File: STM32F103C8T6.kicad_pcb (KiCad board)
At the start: 2 copper layers, 25.4 x 50.8 mm, 29 parts, among them SW1 SW_Push, SW2 SW_Push, U1 STM32F103C8T6, U2 AMS1117-3.3

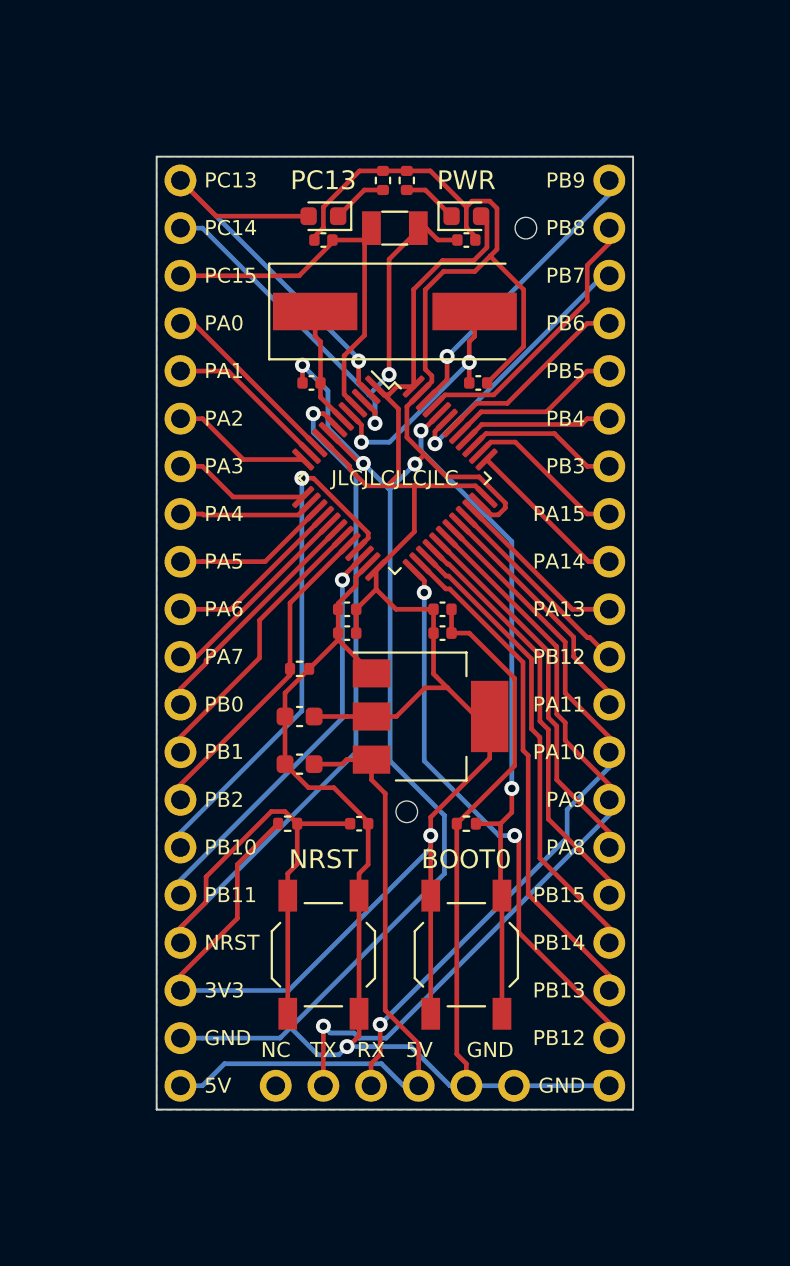
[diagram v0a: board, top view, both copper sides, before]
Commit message: Update to KiCAD 7.0
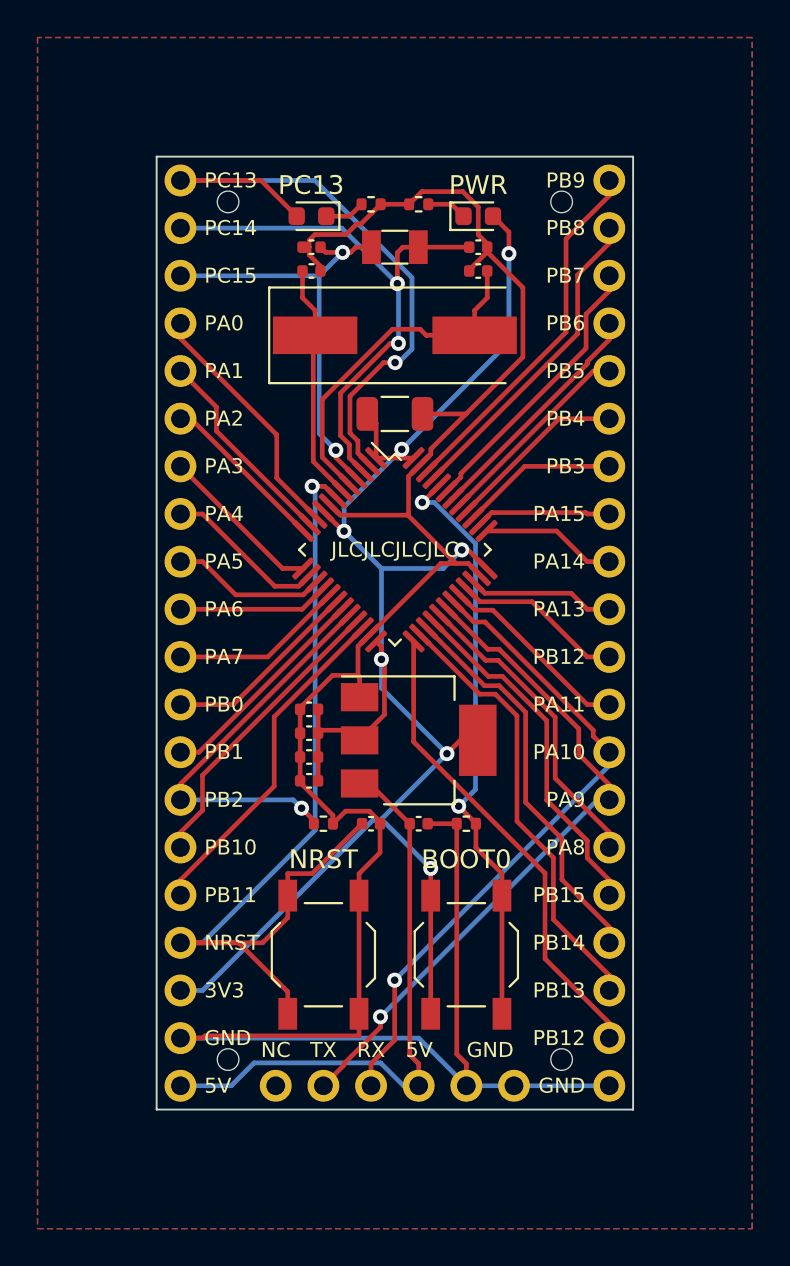
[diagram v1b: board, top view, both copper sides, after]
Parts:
- removed R3: 10KΩ, Resistor_SMD:R_0402_1005Metric
- added H3: MountingHole, MountingHole:MountingHole_2.2mm_M2, F.Cu at (130.8, 78.6)
- added H4: MountingHole, MountingHole:MountingHole_2.2mm_M2, F.Cu at (148.6, 124.3)
- C11: value 10μF -> 1μF; footprint Capacitor_SMD:C_0603_1608Metric -> Capacitor_SMD:C_0402_1005Metric
- C12: value 22μF -> 100μF; footprint Capacitor_SMD:C_0603_1608Metric -> Capacitor_SMD:C_1206_3216Metric
- CH1, CH2: value Conn_01x20_Male -> Conn_01x20
- UART1: value Conn_01x06_Male -> Conn_01x06
- moved CH2 48.3 mm to (151.1, 77.5), turned to 180 degrees
- moved C12 16.9 mm to (139.7, 89.9), turned to 0 degrees
- moved H2 16.3 mm to (130.8, 124.3)
- moved C9 10.6 mm to (135.1, 108.2), turned to 180 degrees
- moved C7 9.37 mm to (135.1, 109.5)
- moved R1 8.35 mm to (135.9, 111.8)
- moved C10 8.19 mm to (135.1, 105.7), turned to 180 degrees
- moved C11 7.10 mm to (141.0, 111.8), turned to 0 degrees
- moved C3 5.97 mm to (144.1, 82.3), turned to 0 degrees
- moved C4 5.97 mm to (135.3, 82.3), turned to 180 degrees
- moved C8 5.71 mm to (135.1, 106.9)
- moved U1 3.81 mm to (139.7, 97.2)
- moved H1 2.36 mm to (148.6, 78.6)
- moved R4 1.42 mm to (138.4, 78.7), turned to 0 degrees
- moved R5 1.42 mm to (141.0, 78.7), turned to 180 degrees
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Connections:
- CH2 pad 1: GND -> PB9
- CH2 pad 10: PA12 -> PA13
- CH2 pad 11: PA13 -> PA12
- CH2 pad 12: PA14 -> PA11
- CH2 pad 13: PA15 -> PA10
- CH2 pad 14: PB3 -> PA9
- CH2 pad 15: PB4 -> PA8
- CH2 pad 16: PB5 -> PB15
- CH2 pad 17: PB6 -> PB14
- CH2 pad 18: PB7 -> PB13
- CH2 pad 19: PB8 -> PB12
- CH2 pad 2: PB12 -> PB8
- CH2 pad 20: PB9 -> GND
- CH2 pad 3: PB13 -> PB7
- CH2 pad 4: PB14 -> PB6
- CH2 pad 5: PB15 -> PB5
- CH2 pad 6: PA8 -> PB4
- CH2 pad 7: PA9 -> PB3
- CH2 pad 8: PA10 -> PA15
- CH2 pad 9: PA11 -> PA14
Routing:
- net GND: track 182.3 -> 130.5 mm, vias 4 -> 0
- net PB10: track 28.3 -> 15.9 mm, vias 1 -> 0
- net +3.3V: track 103.7 -> 93.1 mm, vias 1 -> 7
- net PC13: track 23.1 -> 33.7 mm
- net NRST: track 58.3 -> 51.3 mm
- net PD1: track 6.38 -> 13.4 mm
- net PA9: track 42.0 -> 36.1 mm
- net PD0: track 13.3 -> 18.7 mm, vias 2 -> 0
- net BOOT0: track 36.1 -> 31.5 mm
- net PB12: track 29.8 -> 25.5 mm, vias 2 -> 0
- net PB2: track 17.4 -> 21.3 mm, vias 0 -> 1
- net +5V: track 35.3 -> 31.4 mm
- net PB11: track 22.1 -> 18.3 mm, vias 1 -> 0
- net PB9: track 15.7 -> 19.5 mm, vias 1 -> 0
- net PA10: track 38.3 -> 34.9 mm
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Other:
- board text removed: "STM32F103C8T6"

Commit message: Add files via upload
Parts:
- removed H1, H2, H3, H4: MountingHole, MountingHole:MountingHole_2.2mm_M2
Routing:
- net GND: track 130.5 -> 129.8 mm
- net PC13: track 33.7 -> 34.5 mm
